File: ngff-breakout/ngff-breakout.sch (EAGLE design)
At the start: 74 parts, among them U2 LD1085D2T33R, X1 PINHD-2X4, X7 694108106102, X9 ZX360D-B-10P(30), Y4 MHF4, Y5 MHF4, Y6 MHF4

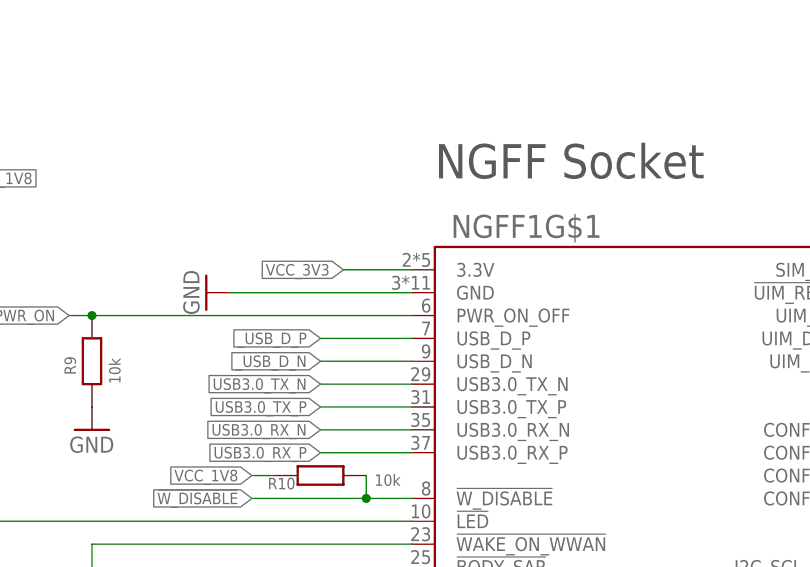
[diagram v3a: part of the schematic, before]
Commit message: ngff: repair M.2/NGFF footprint (see SYS#4661)
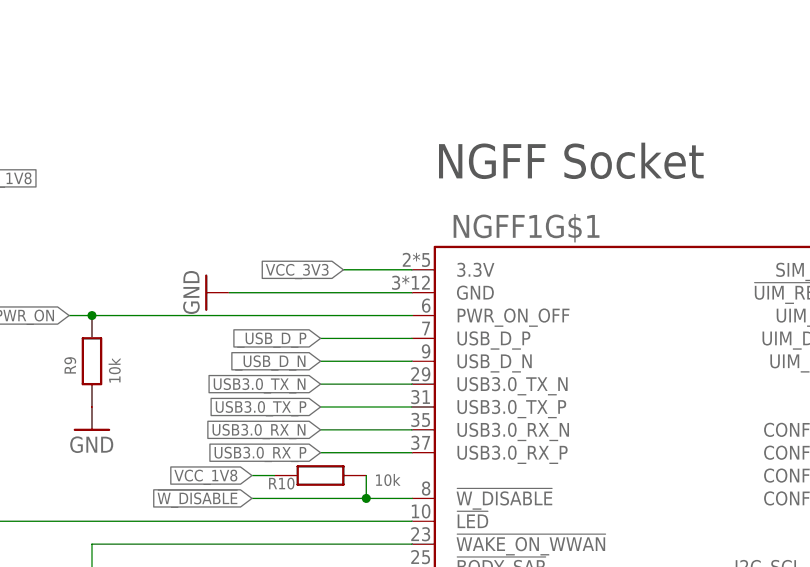
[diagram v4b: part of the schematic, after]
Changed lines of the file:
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@@
 <layer number="98" name="Guide" color="6" fill="1" visible="yes" active="yes"/>
 <layer number="99" name="SpiceOrder" color="7" fill="1" visible="no" active="no"/>
-<layer number="105" name="Beschreib" color="9" fill="1" visible="no" active="no"/>
-<layer number="106" name="BGA-Top" color="4" fill="1" visible="no" active="no"/>
-<layer number="107" name="BD-Top" color="5" fill="1" visible="no" active="no"/>
-<layer number="113" name="Laser Schnitt" color="12" fill="1" visible="no" active="no"/>
-<layer number="114" name="Laser Fläche Gravur" color="15" fill="1" visible="no" active="no"/>
-<layer number="115" name="Laser Bohrungen" color="9" fill="1" visible="no" active="no"/>
-<layer number="118" name="Rect_Pads" color="7" fill="1" visible="no" active="no"/>
-<layer number="133" name="Ritzung" color="1" fill="0" visible="no" active="no"/>
-<layer number="134" name="Fräsung" color="2" fill="0" visible="no" active="no"/>
-<layer number="142" name="BMRestrict" color="1" fill="9" visible="no" active="no"/>
-<layer number="148" name="Document_mirrored" color="7" fill="1" visible="no" active="no"/>
-<layer number="151" name="HeatSink" color="14" fill="1" visible="no" active="no"/>
-<layer number="156" name="gesam-Maß" color="1" fill="7" visible="no" active="no"/>
-<layer number="157" name="FaceMchng" color="3" fill="1" visible="no" active="no"/>
-<layer number="158" name="FaceMMeas" color="3" fill="1" visible="no" active="no"/>
-<layer number="159" name="Geh-Bear2" color="1" fill="7" visible="no" active="no"/>
-<layer number="170" name="ProgrammierAdapter" color="7" fill="1" visible="no" active="no"/>
-<layer number="200" name="200bmp" color="1" fill="10" visible="no" active="no"/>
-<layer number="201" name="201bmp" color="2" fill="1" visible="no" active="no"/>
-<layer number="217" name="217bmp" color="18" fill="1" visible="no" active="no"/>
-<layer number="218" name="218bmp" color="19" fill="1" visible="no" active="no"/>
-<layer number="219" name="219bmp" color="20" fill="1" visible="no" active="no"/>
-<layer number="220" name="220bmp" color="21" fill="1" visible="no" active="no"/>
-<layer number="221" name="221bmp" color="22" fill="1" visible="no" active="no"/>
-<layer number="222" name="222bmp" color="23" fill="1" visible="no" active="no"/>
-<layer number="223" name="223bmp" color="24" fill="1" visible="no" active="no"/>
-<layer number="224" name="224bmp" color="25" fill="1" visible="no" active="no"/>
-<layer number="232" name="Eagle3D_PG2" color="7" fill="1" visible="no" active="no"/>
-<layer number="233" name="Eagle3D_PG3" color="7" fill="1" visible="no" active="no"/>
-<layer number="250" name="Descript" color="3" fill="1" visible="no" active="no"/>
-<layer number="251" name="SMDround" color="12" fill="11" visible="no" active="no"/>
-<layer number="254" name="OrgLBR" color="13" fill="1" visible="no" active="no"/>
 </layers>
 <schematic xreflabel="%F%N/%S.%C%R" xrefpart="/%S.%C%R">
@@
 </class>
 <class number="3" name="supply" width="0.6" drill="0">
-<clearance class="0" value="0.254"/>
+<clearance class="0" value="0.3"/>
 </class>
 </classes>

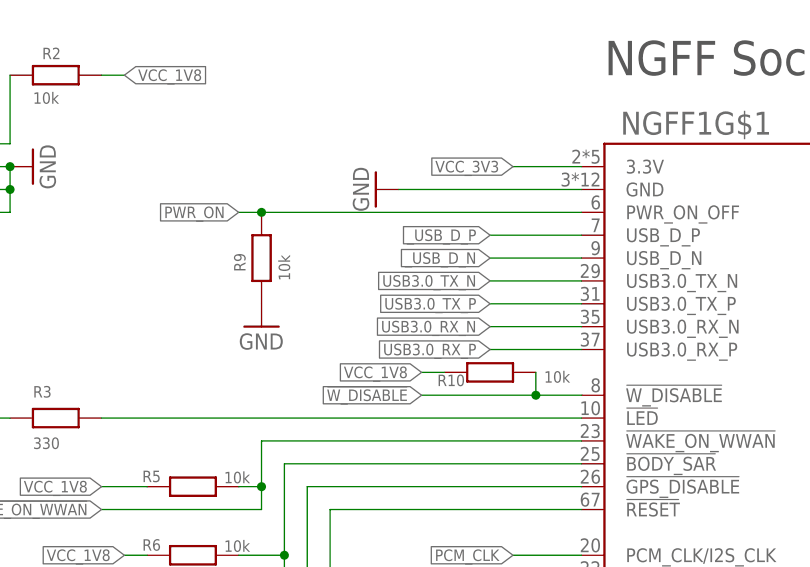
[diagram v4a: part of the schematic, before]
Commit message: ngff: set R9 to 100k (solves OS#4209)
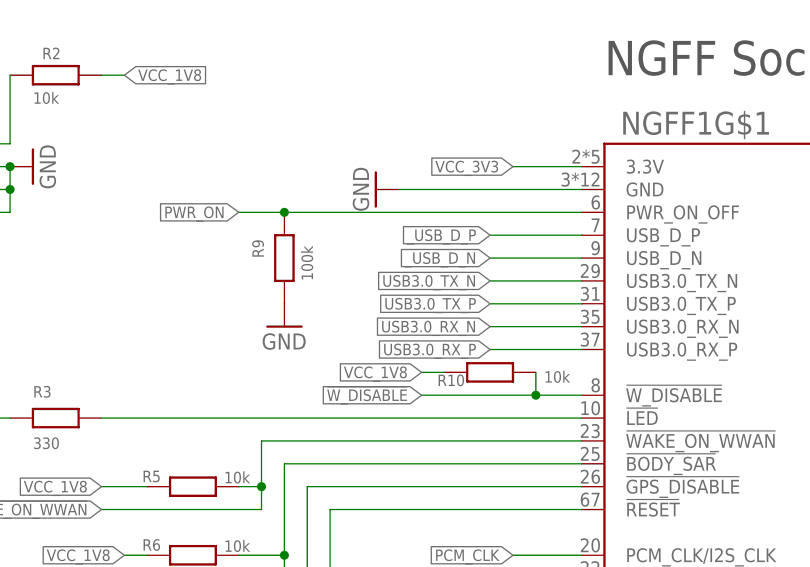
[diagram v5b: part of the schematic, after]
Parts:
- R9: value 10k -> 100k; DESCRIPTION RES 10K OHM 1%% 1/10W 0603 -> RES SMD 100K OHM 1%% 1/10W 0603; LINK https://www.digikey.de/product-detail/de/stackpole-electron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 -> https://www.digikey.de/product-detail/de/vishay-dale/CRCW06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; MANUFACTURER Stackpole Electronics Inc -> Vishay Dale; MANUFACTURERPARTNUMBER RMCF0603FT10K0 -> CRCW0603100KFKEA; ROHSCERTIFICATE UNKNOWN ROHS CERTIFICATE -> Bleifrei / RoHS-konform; SOURCEPARTNUMBER RMCF0603FT10K0CT-ND -> 541-100KHCT-ND
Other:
- moved on the sheet: R9

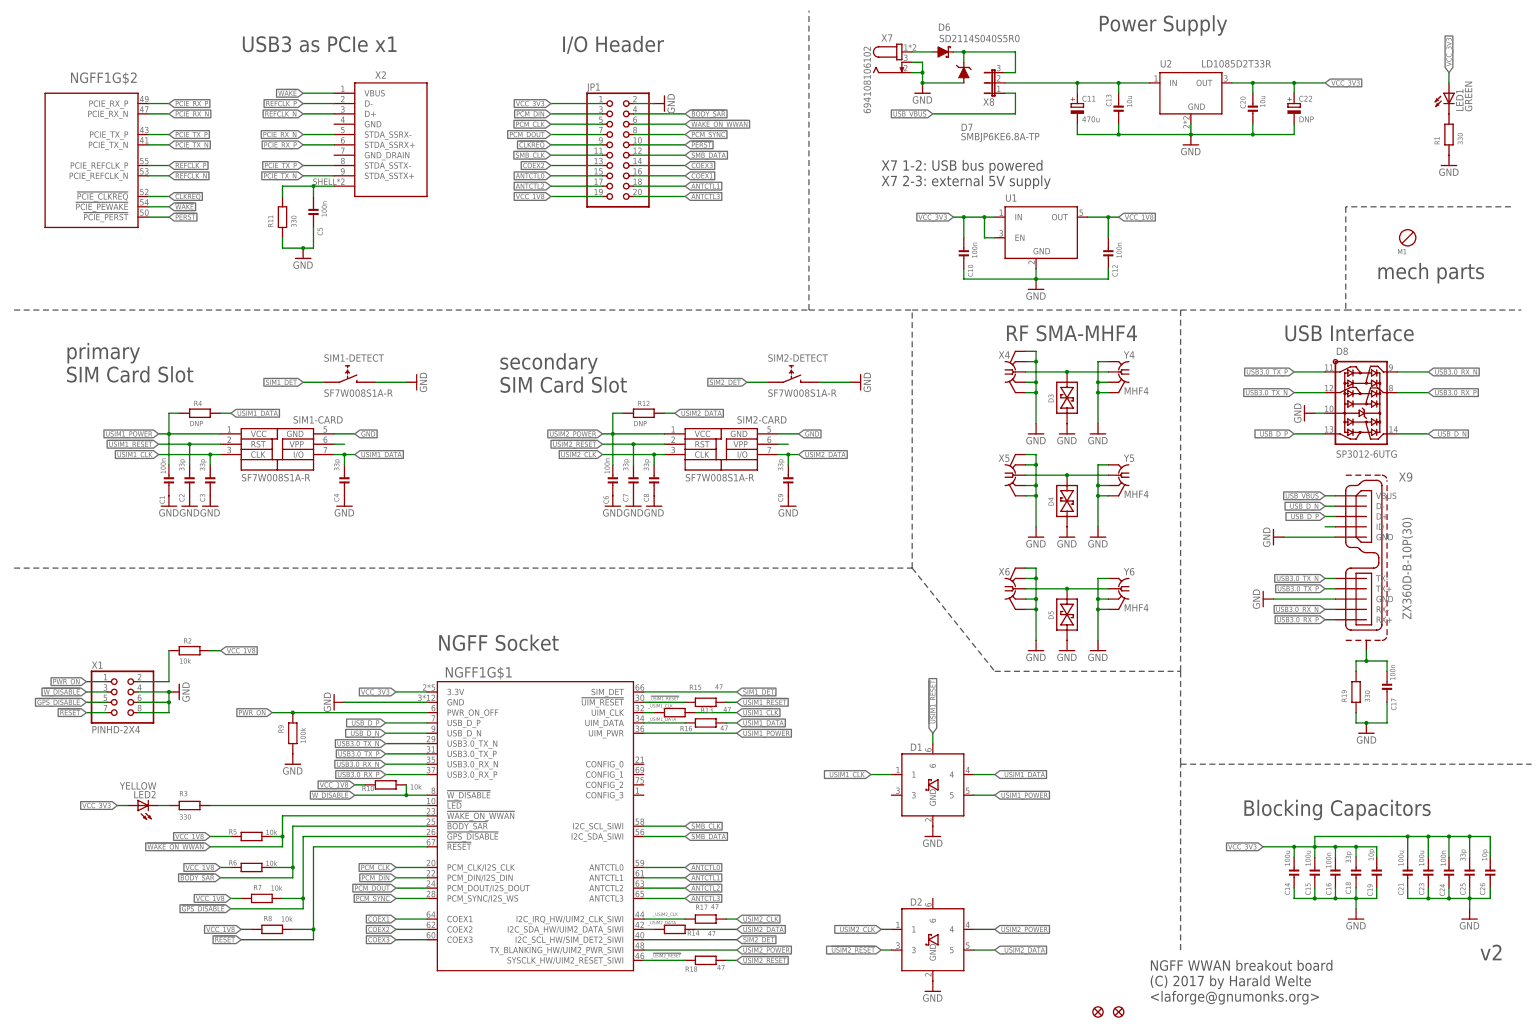
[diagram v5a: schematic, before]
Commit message: ngff: move PCIe header 3mm inwards (solves OS#4210)
... and started OS#4211.
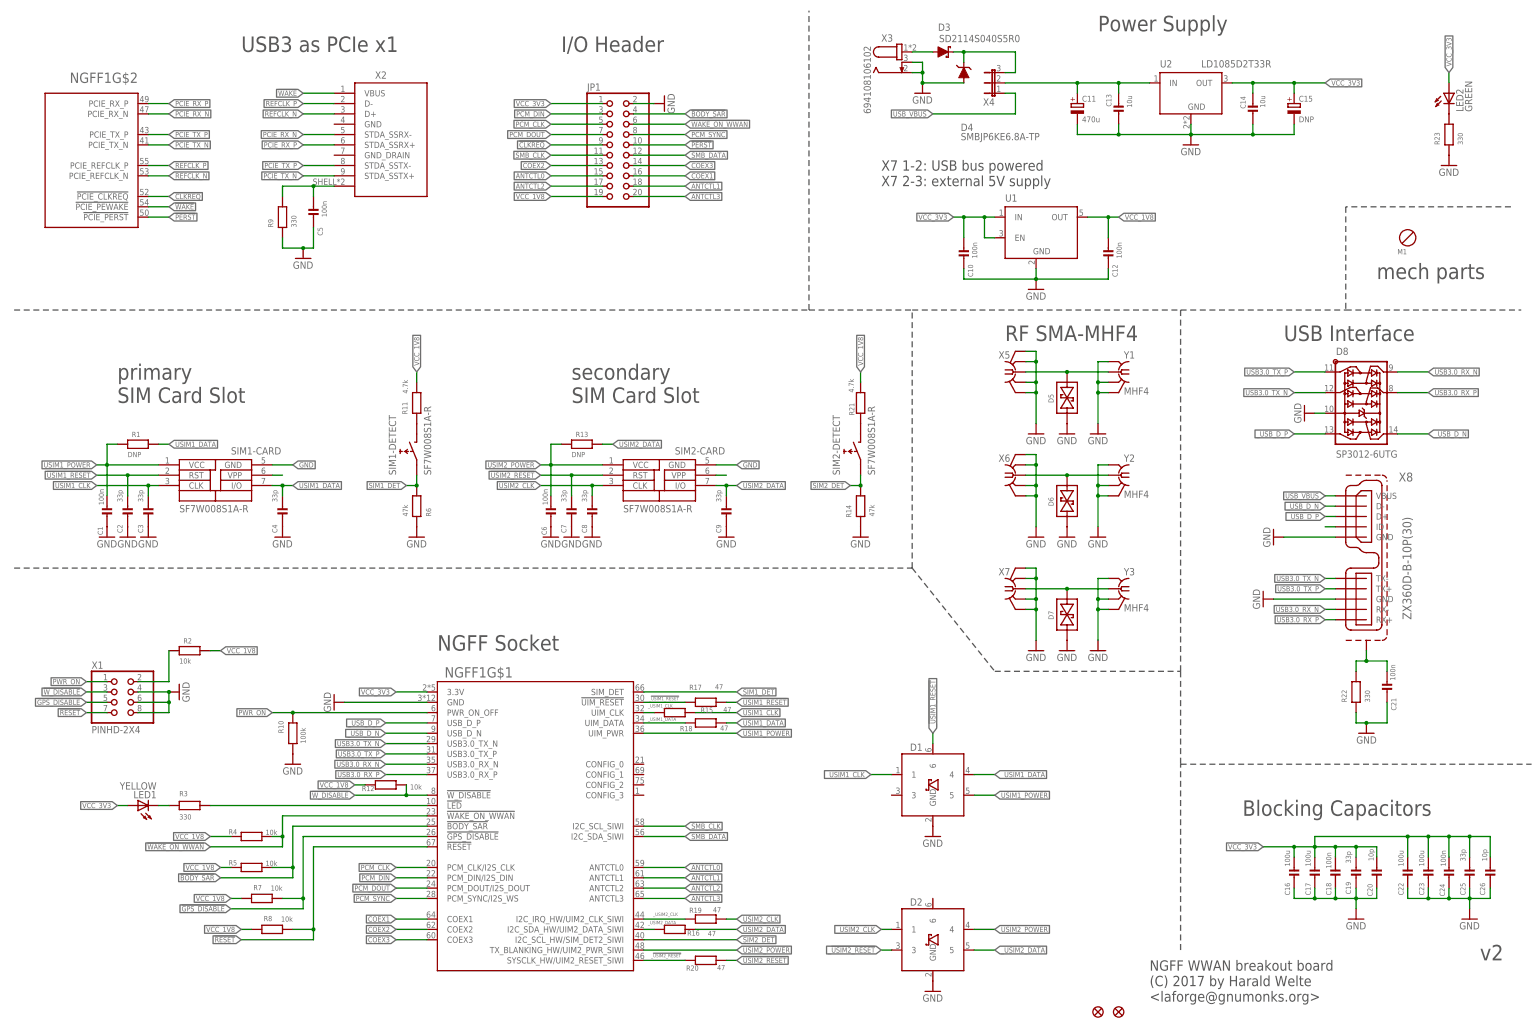
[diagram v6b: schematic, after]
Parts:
- removed X9: ZX360D-B-10P(30), USB30-MICROB:USB3.0-MICROB
- added R20: 47, rc-sysmocom:RESISTOR_0402
- added R21: 4.7k, rc-sysmocom:RESISTOR_0603
- added R22, R23: 330, rc-sysmocom:RESISTOR_0603
- added X3: 694108106102, Wurth_Elektronik_Electromechanic_DC_Power_Jack_Connectors_rev15c:694108106102
- C14: value 100u -> 10u; device rc-sysmocom:CAP_CERAMIC1206 -> rc-sysmocom:CAP_CERAMIC_0805; DESCRIPTION CAP CER 100UF 6.3V X5R 1206 -> CAP CER 10UF 16V X5R 0805; LINK http://www.digikey.de/product-detail/de/murata-electronics-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 -> http://www.digikey.de/product-detail/de/samsung-electro-mec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; MANUFACTURER Murata Electronics North America -> Samsung Electro-Mechanics; MANUFACTURERPARTNUMBER GRM31CR60J107ME39K -> CL21A106KOQNNNG; SOURCEPARTNUMBER 490-7217-1-ND -> 1276-6455-1-ND
- C15: value 100u -> DNP; device rc-sysmocom:CAP_CERAMIC1206 -> rcl:CPOL-EUSMCE; DESCRIPTION CAP CER 100UF 6.3V X5R 1206 -> NO DESCRIPTION; LINK http://www.digikey.de/product-detail/de/murata-electronics-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 -> UNKNOWN LINK; MANUFACTURER Murata Electronics North America -> UNKNOWN MANUFACTURER; MANUFACTURERPARTNUMBER GRM31CR60J107ME39K -> UNKNOWN MANUFACTURER PART NUMBER; POPULATED TRUE -> FALSE; ROHSCERTIFICATE Bleifrei / RoHS-konform -> UNKNOWN ROHS CERTIFICATE; SOURCE DIGIKEY -> UNKNOWN SOURCE; SOURCEPARTNUMBER 490-7217-1-ND -> UNKNOWN SOURCE PART NUMBER
- C16, C17: value 100n -> 100u; device rc-sysmocom:CAP_CERAMIC_0603 -> rc-sysmocom:CAP_CERAMIC1206; DESCRIPTION CAP CER 0.1UF 16V 10% X7R 0603 -> CAP CER 100UF 6.3V X5R 1206; LINK http://www.digikey.de/product-detail/de/foo/1276-1005-1-ND -> http://www.digikey.de/product-detail/de/murata-electronics-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; MANUFACTURER Samsung Electro-Mechanics America, Inc -> Murata Electronics North America; MANUFACTURERPARTNUMBER CL10B104KO8NNNC -> GRM31CR60J107ME39K; SOURCEPARTNUMBER 1276-1005-1-ND -> 490-7217-1-ND
- C18: value 33p -> 100n; device rc-sysmocom:CAP_CERAMIC_0402 -> rc-sysmocom:CAP_CERAMIC_0603; DESCRIPTION CAP CER 33PF 50V NP0 0402 -> CAP CER 0.1UF 16V 10% X7R 0603; LINK http://www.digikey.de/product-detail/de/CL05C330JB5NNNC/127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 -> http://www.digikey.de/product-detail/de/foo/1276-1005-1-ND; MANUFACTURER Samsung Electro-Mechanics America, Inc. -> Samsung Electro-Mechanics America, Inc; MANUFACTURERPARTNUMBER CL05C330JB5NNNC -> CL10B104KO8NNNC; SOURCEPARTNUMBER 1276-1272-1-ND -> 1276-1005-1-ND
- C19: value 10p -> 33p; device rc-sysmocom:CAP_CERAMIC_0603 -> rc-sysmocom:CAP_CERAMIC_0402; DESCRIPTION CAP CER 10PF 50V NP0 0603 -> CAP CER 33PF 50V NP0 0402; LINK http://www.digikey.de/product-detail/de/C0603C100J5GACTU/39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 -> http://www.digikey.de/product-detail/de/CL05C330JB5NNNC/127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; MANUFACTURER Kemet -> Samsung Electro-Mechanics America, Inc.; MANUFACTURERPARTNUMBER C0603C100J5GACTU -> CL05C330JB5NNNC; SOURCEPARTNUMBER 399-1049-1-ND -> 1276-1272-1-ND
- C20: value 10u -> 10p; device rc-sysmocom:CAP_CERAMIC_0805 -> rc-sysmocom:CAP_CERAMIC_0603; DESCRIPTION CAP CER 10UF 16V X5R 0805 -> CAP CER 10PF 50V NP0 0603; LINK http://www.digikey.de/product-detail/de/samsung-electro-mec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 -> http://www.digikey.de/product-detail/de/C0603C100J5GACTU/39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; MANUFACTURER Samsung Electro-Mechanics -> Kemet; MANUFACTURERPARTNUMBER CL21A106KOQNNNG -> C0603C100J5GACTU; SOURCEPARTNUMBER 1276-6455-1-ND -> 399-1049-1-ND
- C21: value 100u -> 100n; device rc-sysmocom:CAP_CERAMIC1206 -> rc-sysmocom:CAP_CERAMIC_0603; DESCRIPTION CAP CER 100UF 6.3V X5R 1206 -> CAP CER 0.1UF 16V 10% X7R 0603; LINK http://www.digikey.de/product-detail/de/murata-electronics-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 -> http://www.digikey.de/product-detail/de/foo/1276-1005-1-ND; MANUFACTURER Murata Electronics North America -> Samsung Electro-Mechanics America, Inc; MANUFACTURERPARTNUMBER GRM31CR60J107ME39K -> CL10B104KO8NNNC; SOURCEPARTNUMBER 490-7217-1-ND -> 1276-1005-1-ND
- C22: value DNP -> 100u; device rcl:CPOL-EUSMCE -> rc-sysmocom:CAP_CERAMIC1206; DESCRIPTION NO DESCRIPTION -> CAP CER 100UF 6.3V X5R 1206; LINK UNKNOWN LINK -> http://www.digikey.de/product-detail/de/murata-electronics-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; MANUFACTURER UNKNOWN MANUFACTURER -> Murata Electronics North America; MANUFACTURERPARTNUMBER UNKNOWN MANUFACTURER PART NUMBER -> GRM31CR60J107ME39K; POPULATED FALSE -> TRUE; ROHSCERTIFICATE UNKNOWN ROHS CERTIFICATE -> Bleifrei / RoHS-konform; SOURCE UNKNOWN SOURCE -> DIGIKEY; SOURCEPARTNUMBER UNKNOWN SOURCE PART NUMBER -> 490-7217-1-ND
- D3: value GG040205170N2P -> SD2114S040S5R0; device diodes-sysmocom:TVSDIODE-BIDI-0402 -> diodes-sysmocom:DIODE-SCHOTTKY-SMB; DESCRIPTION TVS DIODE 5V 10V 0402 -> DIODE SCHOTTKY 40V 5A SMB; LINK https://www.digikey.de/product-detail/de/avx-corporation/GG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 -> https://www.digikey.de/product-detail/de/avx-corporation/SD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; MANUFACTURERPARTNUMBER GG040205170N2P -> SD2114S040S5R0; ROHSCERTIFICATE Bleifrei / RoHS-konform -> UNKNOWN ROHS CERTIFICATE; SOURCEPARTNUMBER 478-10595-1-ND -> 478-7816-1-ND
- D4: value GG040205170N2P -> SMBJP6KE6.8A-TP; device diodes-sysmocom:TVSDIODE-BIDI-0402 -> diodes-sysmocom:DIODE-TVS-SMB; DESCRIPTION TVS DIODE 5V 10V 0402 -> TVS DIODE 5.8V 10.5V DO214AA; LINK https://www.digikey.de/product-detail/de/avx-corporation/GG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 -> https://www.digikey.de/product-detail/de/micro-commercial-c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; MANUFACTURER AVX Corporation -> Micro Commercial Co; MANUFACTURERPARTNUMBER GG040205170N2P -> SMBJP6KE6.8A-TP; SOURCEPARTNUMBER 478-10595-1-ND -> SMBJP6KE6.8A-TPMSCT-ND
- D6: value SD2114S040S5R0 -> GG040205170N2P; device diodes-sysmocom:DIODE-SCHOTTKY-SMB -> diodes-sysmocom:TVSDIODE-BIDI-0402; DESCRIPTION DIODE SCHOTTKY 40V 5A SMB -> TVS DIODE 5V 10V 0402; LINK https://www.digikey.de/product-detail/de/avx-corporation/SD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 -> https://www.digikey.de/product-detail/de/avx-corporation/GG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; MANUFACTURERPARTNUMBER SD2114S040S5R0 -> GG040205170N2P; ROHSCERTIFICATE UNKNOWN ROHS CERTIFICATE -> Bleifrei / RoHS-konform; SOURCEPARTNUMBER 478-7816-1-ND -> 478-10595-1-ND
- D7: value SMBJP6KE6.8A-TP -> GG040205170N2P; device diodes-sysmocom:DIODE-TVS-SMB -> diodes-sysmocom:TVSDIODE-BIDI-0402; DESCRIPTION TVS DIODE 5.8V 10.5V DO214AA -> TVS DIODE 5V 10V 0402; LINK https://www.digikey.de/product-detail/de/micro-commercial-c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 -> https://www.digikey.de/product-detail/de/avx-corporation/GG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; MANUFACTURER Micro Commercial Co -> AVX Corporation; MANUFACTURERPARTNUMBER SMBJP6KE6.8A-TP -> GG040205170N2P; SOURCEPARTNUMBER SMBJP6KE6.8A-TPMSCT-ND -> 478-10595-1-ND
- LED1: value GREEN -> YELLOW
- LED2: value YELLOW -> GREEN
- R1: value 330 -> DNP; DESCRIPTION RES SMD 330 OHM 5%% 1/10W 0603 -> RES 10K OHM 1%% 1/10W 0603; LINK http://www.digikey.de/product-detail/de/yageo/RC0603JR-0733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 -> https://www.digikey.de/product-detail/de/stackpole-electron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; MANUFACTURER Yageo -> Stackpole Electronics Inc; MANUFACTURERPARTNUMBER RC0603JR-07330RL -> RMCF0603FT10K0; ROHSCERTIFICATE Bleifrei / RoHS-konform -> UNKNOWN ROHS CERTIFICATE; SOURCEPARTNUMBER 311-330GRCT-ND -> RMCF0603FT10K0CT-ND
- R10: value 10k -> 100k; DESCRIPTION RES 10K OHM 1%% 1/10W 0603 -> RES SMD 100K OHM 1%% 1/10W 0603; LINK https://www.digikey.de/product-detail/de/stackpole-electron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 -> https://www.digikey.de/product-detail/de/vishay-dale/CRCW06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; MANUFACTURER Stackpole Electronics Inc -> Vishay Dale; MANUFACTURERPARTNUMBER RMCF0603FT10K0 -> CRCW0603100KFKEA; ROHSCERTIFICATE UNKNOWN ROHS CERTIFICATE -> Bleifrei / RoHS-konform; SOURCEPARTNUMBER RMCF0603FT10K0CT-ND -> 541-100KHCT-ND
- R11: value 330 -> 4.7k; DESCRIPTION RES SMD 330 OHM 5%% 1/10W 0603 -> RES SMD 4.7K OHM 5% 1/10W 0603; LINK http://www.digikey.de/product-detail/de/yageo/RC0603JR-0733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 -> http://www.digikey.de/product-detail/de/RC0603JR-074K7L/311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; MANUFACTURERPARTNUMBER RC0603JR-07330RL -> RC0603JR-074K7L; SOURCEPARTNUMBER 311-330GRCT-ND -> 311-4.7KGRCT-ND
- R12, R4: value DNP -> 10k
- R13: value 47 -> DNP; device rc-sysmocom:RESISTOR_0402 -> rc-sysmocom:RESISTOR_0603; DESCRIPTION RES SMD 47 OHM 5%% 1/10W 0603 -> RES 10K OHM 1%% 1/10W 0603; LINK http://www.digikey.de/product-detail/de/yageo/RC0603JR-0747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 -> https://www.digikey.de/product-detail/de/stackpole-electron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; MANUFACTURER Yageo -> Stackpole Electronics Inc; MANUFACTURERPARTNUMBER RC0603JR-0747RL -> RMCF0603FT10K0; ROHSCERTIFICATE Bleifrei / RoHS-konform -> UNKNOWN ROHS CERTIFICATE; SOURCEPARTNUMBER 311-47GRCT-ND -> RMCF0603FT10K0CT-ND
- R14: value 47 -> 47k; device rc-sysmocom:RESISTOR_0402 -> rc-sysmocom:RESISTOR_0603; DESCRIPTION RES SMD 47 OHM 5%% 1/10W 0603 -> RES 47K OHM 1%% 1/10W 0603; LINK http://www.digikey.de/product-detail/de/yageo/RC0603JR-0747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 -> https://www.digikey.de/product-detail/de/stackpole-electron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; MANUFACTURER Yageo -> Stackpole Electronics Inc; MANUFACTURERPARTNUMBER RC0603JR-0747RL -> RMCF0603FT47K0; SOURCEPARTNUMBER 311-47GRCT-ND -> RMCF0603FT47K0CT-ND
- R15: DESCRIPTION CRGCQ 0402 47R 1%% -> RES SMD 47 OHM 5%% 1/10W 0603; LINK https://www.digikey.de/product-detail/de/te-connectivity-pa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 -> http://www.digikey.de/product-detail/de/yageo/RC0603JR-0747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; MANUFACTURER TE Connectivity Passive Product -> Yageo; MANUFACTURERPARTNUMBER CRGCQ0402F47R -> RC0603JR-0747RL; ROHSCERTIFICATE UNKNOWN ROHS CERTIFICATE -> Bleifrei / RoHS-konform; SOURCEPARTNUMBER A129611CT-ND -> 311-47GRCT-ND
- R17: DESCRIPTION RES SMD 47 OHM 5%% 1/10W 0603 -> CRGCQ 0402 47R 1%%; LINK http://www.digikey.de/product-detail/de/yageo/RC0603JR-0747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 -> https://www.digikey.de/product-detail/de/te-connectivity-pa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; MANUFACTURER Yageo -> TE Connectivity Passive Product; MANUFACTURERPARTNUMBER RC0603JR-0747RL -> CRGCQ0402F47R; ROHSCERTIFICATE Bleifrei / RoHS-konform -> UNKNOWN ROHS CERTIFICATE; SOURCEPARTNUMBER 311-47GRCT-ND -> A129611CT-ND
- R19: value 330 -> 47; device rc-sysmocom:RESISTOR_0603 -> rc-sysmocom:RESISTOR_0402; DESCRIPTION RES SMD 330 OHM 5%% 1/10W 0603 -> RES SMD 47 OHM 5%% 1/10W 0603; LINK http://www.digikey.de/product-detail/de/yageo/RC0603JR-0733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 -> http://www.digikey.de/product-detail/de/yageo/RC0603JR-0747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; MANUFACTURERPARTNUMBER RC0603JR-07330RL -> RC0603JR-0747RL; SOURCEPARTNUMBER 311-330GRCT-ND -> 311-47GRCT-ND
- R6: value 10k -> 47k; DESCRIPTION RES 10K OHM 1%% 1/10W 0603 -> RES 47K OHM 1%% 1/10W 0603; LINK https://www.digikey.de/product-detail/de/stackpole-electronics-inc/RMCF0603FT10K0/RMCF0603FT10K0CT-ND -> https://www.digikey.de/product-detail/de/stackpole-electronics-inc/RMCF0603FT47K0/RMCF0603FT47K0CT-ND; MANUFACTURERPARTNUMBER RMCF0603FT10K0 -> RMCF0603FT47K0; ROHSCERTIFICATE UNKNOWN ROHS CERTIFICATE -> Bleifrei / RoHS-konform; SOURCEPARTNUMBER RMCF0603FT10K0CT-ND -> RMCF0603FT47K0CT-ND
- R9: value 100k -> 330; DESCRIPTION RES SMD 100K OHM 1%% 1/10W 0603 -> RES SMD 330 OHM 5%% 1/10W 0603; LINK https://www.digikey.de/product-detail/de/vishay-dale/CRCW06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 -> http://www.digikey.de/product-detail/de/yageo/RC0603JR-0733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; MANUFACTURER Vishay Dale -> Yageo; MANUFACTURERPARTNUMBER CRCW0603100KFKEA -> RC0603JR-07330RL; SOURCEPARTNUMBER 541-100KHCT-ND -> 311-330GRCT-ND
- X4: device laforge:SMA-F-S-TH -> jumper:JP2E; CLASS CONNECTOR -> CONNECTOR\JUMPER; DESCRIPTION CONN SMA JACK STR 50 OHM PCB -> NO DESCRIPTION; LINK http://www.digikey.de/product-detail/de/te-connectivity-amp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 -> UNKNOWN LINK; MANUFACTURER TE Connectivity AMP Connectors -> UNKNOWN MANUFACTURER; MANUFACTURERPARTNUMBER 5-1814832-1 -> UNKNOWN MANUFACTURER PART NUMBER; ROHSCERTIFICATE Bleifrei / RoHS-konform -> UNKNOWN ROHS CERTIFICATE; SOURCE DIGIKEY -> UNKNOWN SOURCE; SOURCEPARTNUMBER A97594-ND -> UNKNOWN SOURCE PART NUMBER
- X7: value 694108106102 -> (none); device Wurth_Elektronik_Electromechanic_DC_Power_Jack_Connectors_rev15c:694108106102 -> laforge:SMA-F-S-TH; CLASS RELAY -> CONNECTOR; DESCRIPTION CONN PWR JACK 2.5X5.5MM SOLDER -> CONN SMA JACK STR 50 OHM PCB; LINK http://www.digikey.de/product-detail/de/wurth-electronics-i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 -> http://www.digikey.de/product-detail/de/te-connectivity-amp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; MANUFACTURER Wurth Electronics Inc. -> TE Connectivity AMP Connectors; MANUFACTURERPARTNUMBER 694108106102 -> 5-1814832-1; SOURCEPARTNUMBER 732-5933-1-ND -> A97594-ND
- X8: value (none) -> ZX360D-B-10P(30); device jumper:JP2E -> USB30-MICROB:USB3.0-MICROB; CLASS CONNECTOR\JUMPER -> CAPACITOR; DESCRIPTION NO DESCRIPTION -> CONN RCPT USB3.0 MICRO B SMD R/A; LINK UNKNOWN LINK -> https://www.digikey.de/product-detail/de/hirose-electric-co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; MANUFACTURER UNKNOWN MANUFACTURER -> Hirose Electric Co Ltd; MANUFACTURERPARTNUMBER UNKNOWN MANUFACTURER PART NUMBER -> ZX360D-B-10P(30); ROHSCERTIFICATE UNKNOWN ROHS CERTIFICATE -> Bleifrei / RoHS-konform; SOURCE UNKNOWN SOURCE -> DIGIKEY; SOURCEPARTNUMBER UNKNOWN SOURCE PART NUMBER -> H125269DKR-ND
- renumbered JP501 to JP2, JP502 to JP3, Y4 to Y1, Y5 to Y2, Y6 to Y3
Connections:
- new net N$11: R21.2, SIM2-DETECT.1@A
- new net N$9: R11.2, SIM1-DETECT.1@A
- net !BODY_SAR: now also R5.1; no longer R6.1
- net !USIM1_RESET: now also R17.2; no longer R15.2
- net !USIM2_RESET: now also R20.2; no longer R18.2
- net !WAKE_ON_WWAN: now also R4.1; no longer R5.1
- net !W_DISABLE: now also R12.1; no longer R10.1
- net GND: now also C15.-, C18.1, C20.2, C22.1, D4.A, D6.P$1, D7.P$1, R10.1, R14.1, R22.1, R23.1, R6.1, X3.2, X3.3, X7.GND@1, X7.GND@2, X7.GND@3, X7.GND@4, X8.GND@0, X8.GND@1; no longer C15.1, C18.2, C20.1, C22.-, D3.P$1, D4.P$1, D7.A, R1.1, R11.1, R19.1, SIM1-DETECT.1@A, SIM2-DETECT.1@A, X4.GND@1, X4.GND@2, X4.GND@3, X4.GND@4, X7.2, X7.3, X9.GND@0, X9.GND@1
- net LDO_IN: now also X4.2; no longer X8.2
- net N$1: now also LED2.C, R23.2; no longer LED1.C, R1.2
- net N$10: now also C21.2, R22.2, X8.S1; no longer C17.2, R19.2, X9.S1
- net N$12: now also D3.C, D4.C, X4.3; no longer D6.C, D7.C, X8.3
- net N$13: now also D5.P$2, X5.1; no longer D3.P$2, X4.1
- net N$14: now also D6.P$2, X6.1; no longer D4.P$2, X5.1
- net N$17: now also X8.ID; no longer X9.ID
- net N$2: now also LED1.C; no longer LED2.C
- net N$3: now also D3.A, X3.1; no longer D6.A, X7.1
- net N$4: now also R9.2; no longer R11.2
- net N$7: now also D7.P$2, X7.1; no longer D5.P$2, X6.1
- net PWR_ON: now also R10.2; no longer R9.2
- net SIM1_DET: now also R6.2
- net SIM2_DET: now also R14.2
- net USB3.0_RX_N: now also X8.RX-; no longer X9.RX-
- net USB3.0_RX_P: now also X8.RX+; no longer X9.RX+
- net USB3.0_TX_N: now also X8.TX-; no longer X9.TX-
- net USB3.0_TX_P: now also X8.TX+; no longer X9.TX+
- net USB_VBUS: now also X4.1, X8.VBUS; no longer X8.1, X9.VBUS
- net USIM1_CLK: now also R15.2; no longer R13.2
- net USIM1_DATA: now also R1.2, R18.2; no longer R16.2, R4.2
- net USIM1_POWER: now also R1.1; no longer R4.1
- net USIM2_CLK: now also R19.2; no longer R17.2
- net USIM2_DATA: now also R13.2, R16.2; no longer R12.2, R14.2
- net USIM2_POWER: now also R13.1; no longer R12.1
- net VCC_1V8: now also R11.1, R12.2, R21.1, R4.2; no longer R10.2, R6.2
- net VCC_3V3: now also C15.+, C17.2, C18.2, C20.1, C22.2; no longer C15.2, C18.1, C20.2, C21.2, C22.+
- net _!USIM1_RESET: now also R17.1; no longer R15.1
- net _!USIM2_RESET: now also R20.1; no longer R18.1
- net _USB_D_N: now also X8.D-; no longer X9.D-
- net _USB_D_P: now also X8.D+; no longer X9.D+
- net _USIM1_CLK: now also R15.1; no longer R13.1
- net _USIM1_DATA: now also R18.1; no longer R16.1
- net _USIM2_CLK: now also R19.1; no longer R17.1
- net _USIM2_DATA: now also R16.1; no longer R14.1
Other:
- moved on the sheet: C1, C14, C16, C17, C18, C19, C2, C20, C21, C3, C4, C6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
